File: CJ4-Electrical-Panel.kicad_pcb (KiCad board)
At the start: 2 copper layers, 122.4 x 62.5 mm, 43 parts, among them J1 Conn_01x03, J2 Conn_01x03, J3 Conn_01x03, J4 Conn_01x03, J5 Conn_01x03, J6 Conn_01x03, J7 USB_B_Mini, J8 AVR-ISP-6, U1 ATmega32U4-A, Y1 16MHz

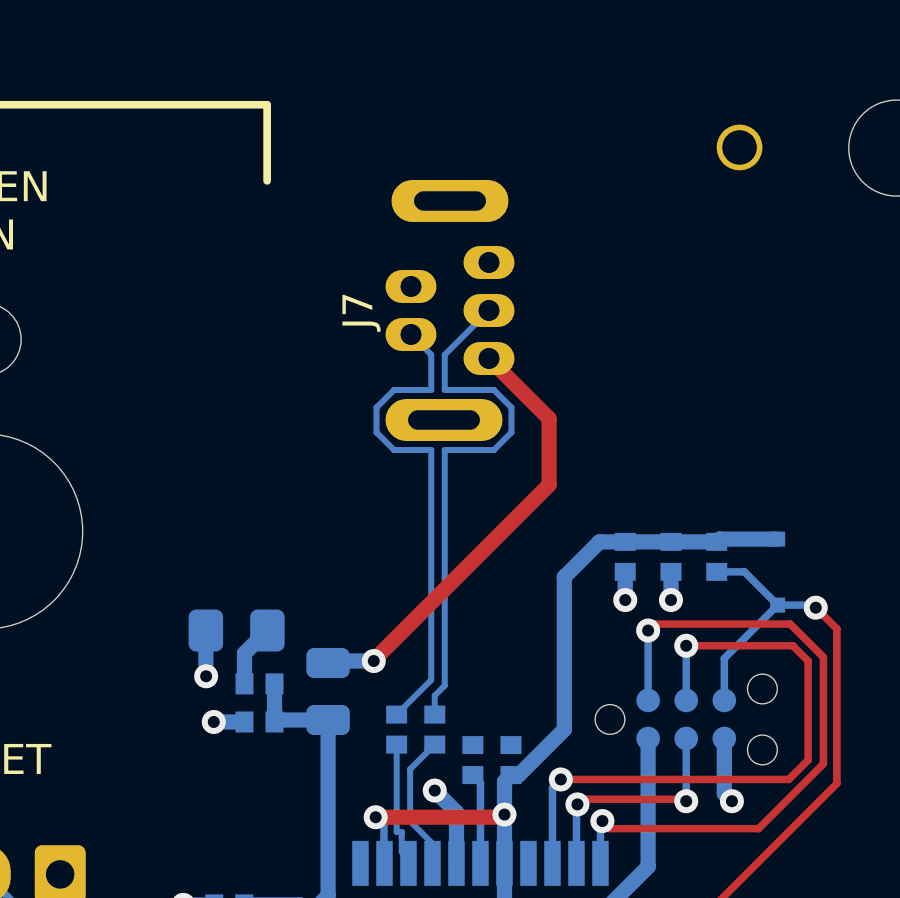
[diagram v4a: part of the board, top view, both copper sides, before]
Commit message: Move USB footprint to back of board
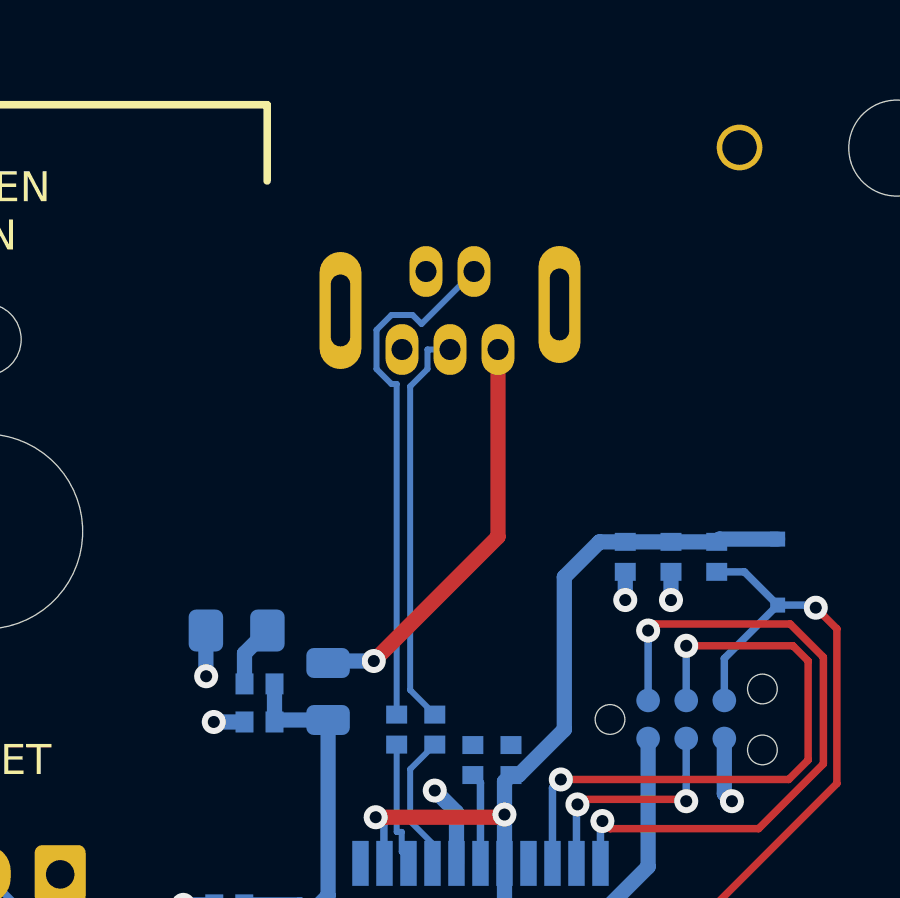
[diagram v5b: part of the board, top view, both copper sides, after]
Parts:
- J7: moved to B.Cu
- turned J7 to 0 degrees
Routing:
- net /DR+: track 18.0 -> 13.5 mm
- net /VBUS: track 14.9 -> 13.7 mm
- net /DR-: track 16.4 -> 17.5 mm
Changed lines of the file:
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@@
     )
-  )
-  (footprint "CJ4-Electrical-Panel:USB_B_Mini_Amphenol_UE25BE5510H" (layer "F.Cu")
-    (at 152.908 61.214 -90)
-    (property "Sheetfile" "CJ4-Electrical-Panel.kicad_sch")
-    (property "Sheetname" "")
-    (attr through_hole)
-    (fp_text reference "J7" (at 0 3.05 90) (layer "F.SilkS")
-      (effects (font (size 1 1) (thickness 0.15)))
-    )
-    (fp_text value "USB_B_Mini" (at 0 -3.25 90) (layer "F.Fab")
-      (effects (font (size 1 1) (thickness 0.15)))
-    )
-    (fp_line (start 3.85 -1.95) (end -3.85 -1.95) (layer "F.CrtYd") (width 0.12))
-    (fp_line (start -3.85 -1.95) (end -3.85 1.95) (layer "F.CrtYd") (width 0.12))
-    (fp_line (start -3.85 1.95) (end 3.85 1.95) (layer "F.CrtYd") (width 0.12))
-    (fp_line (start 3.85 1.95) (end 3.85 -1.95) (layer "F.CrtYd") (width 0.12))
-    (pad "1" thru_hole oval (at 1.6 -1.3 270) (size 1.1 1.7) (drill 0.7) (layers *.Cu *.Mask)
-      (net 32 "/VBUS") (pinfunction "VBUS") (pintype "power_out"))
-    (pad "2" thru_hole oval (at 0.8 1.3 270) (size 1.1 1.7) (drill 0.7) (layers *.Cu *.Mask)
-      (net 30 "/DR-") (pinfunction "D-") (pintype "bidirectional"))
-    (pad "3" thru_hole oval (at 0 -1.3 270) (size 1.1 1.7) (drill 0.7) (layers *.Cu *.Mask)
-      (net 31 "/DR+") (pinfunction "D+") (pintype "bidirectional"))
-    (pad "4" thru_hole oval (at -0.8 1.3 270) (size 1.1 1.7) (drill 0.7) (layers *.Cu *.Mask)
-      (net 29 "unconnected-(J7-Pad4)") (pinfunction "ID") (pintype "passive+no_connect"))
-    (pad "5" thru_hole oval (at -1.6 -1.3 270) (size 1.1 1.7) (drill 0.7) (layers *.Cu *.Mask)
-      (net 2 "GND") (pinfunction "GND") (pintype "power_out"))
-    (pad "6" thru_hole oval (at 3.65 0.2 270) (size 1.4 3.9) (drill oval 0.65 2.4) (layers *.Cu *.Mask)
-      (net 2 "GND") (pinfunction "Shield") (pintype "passive"))
-    (pad "6" thru_hole oval (at -3.65 0 270) (size 1.4 3.9) (drill oval 0.65 2.4) (layers *.Cu *.Mask)
-      (net 2 "GND") (pinfunction "Shield") (pintype "passive"))
   )
   (footprint "CJ4-Electrical-Panel:JLCPCB_Tooling_Hole" (layer "F.Cu")
@@
       (effects (font (size 0.5 0.5) (thickness 0.08)) (justify mirror))
     )
+    (fp_line (start -1.86 -0.96) (end 1 -0.96) (layer "B.SilkS") (width 0.12))
     (fp_line (start -1.86 0.96) (end -1.86 -0.96) (layer "B.SilkS") (width 0.12))
-    (fp_line (start -1.86 -0.96) (end 1 -0.96) (layer "B.SilkS") (width 0.12))
     (fp_line (start 1 0.96) (end -1.86 0.96) (layer "B.SilkS") (width 0.12))
     (fp_line (start -1.85 -0.95) (end -1.85 0.95) (layer "B.CrtYd") (width 0.05))
@@
     )
   )
+  (footprint "CJ4-Electrical-Panel:USB_B_Mini_Amphenol_UE25BE5510H" (layer "B.Cu")
+    (at 152.908 61.214)
+    (property "Sheetfile" "CJ4-Electrical-Panel.kicad_sch")
+    (property "Sheetname" "")
+    (attr through_hole)
+    (fp_text reference "J7" (at 0 -3.05) (layer "B.SilkS")
+      (effects (font (size 1 1) (thickness 0.15)) (justify mirror))
+    )
+    (fp_text value "USB_B_Mini" (at 0 3.25) (layer "B.Fab")
+      (effects (font (size 1 1) (thickness 0.15)) (justify mirror))
+    )
+    (fp_line (start 3.85 1.95) (end -3.85 1.95) (layer "B.CrtYd") (width 0.12))
+    (fp_line (start -3.85 1.95) (end -3.85 -1.95) (layer "B.CrtYd") (width 0.12))
+    (fp_line (start -3.85 -1.95) (end 3.85 -1.95) (layer "B.CrtYd") (width 0.12))
+    (fp_line (start 3.85 -1.95) (end 3.85 1.95) (layer "B.CrtYd") (width 0.12))
+    (pad "1" thru_hole oval (at 1.6 1.3) (size 1.1 1.7) (drill 0.7) (layers *.Cu *.Mask)
+      (net 32 "/VBUS") (pinfunction "VBUS") (pintype "power_out"))
+    (pad "2" thru_hole oval (at 0.8 -1.3) (size 1.1 1.7) (drill 0.7) (layers *.Cu *.Mask)
+      (net 30 "/DR-") (pinfunction "D-") (pintype "bidirectional"))
+    (pad "3" thru_hole oval (at 0 1.3) (size 1.1 1.7) (drill 0.7) (layers *.Cu *.Mask)
+      (net 31 "/DR+") (pinfunction "D+") (pintype "bidirectional"))
+    (pad "4" thru_hole oval (at -0.8 -1.3) (size 1.1 1.7) (drill 0.7) (layers *.Cu *.Mask)
+      (net 29 "unconnected-(J7-Pad4)") (pinfunction "ID") (pintype "passive+no_connect"))
+    (pad "5" thru_hole oval (at -1.6 1.3) (size 1.1 1.7) (drill 0.7) (layers *.Cu *.Mask)
+      (net 2 "GND") (pinfunction "GND") (pintype "power_out"))
+    (pad "6" thru_hole oval (at 3.65 -0.2) (size 1.4 3.9) (drill oval 0.65 2.4) (layers *.Cu *.Mask)
+      (net 2 "GND") (pinfunction "Shield") (pintype "passive"))
+    (pad "6" thru_hole oval (at -3.65 0) (size 1.4 3.9) (drill oval 0.65 2.4) (layers *.Cu *.Mask)
+      (net 2 "GND") (pinfunction "Shield") (pintype "passive"))
+  )
   (footprint "Connector_JST:JST_XH_B3B-XH-A_1x03_P2.50mm_Vertical" (layer "B.Cu")
     (at 139.914 80.01 180)
@@
   (gr_line (start 77.724 54.356) (end 77.724 56.896) (layer "F.SilkS") (width 0.254))
   (gr_line (start 50.8 53.34) (end 50.8 110.744) (layer "Edge.Cuts") (width 0.1))
+  (gr_line (start 53.34 113.284) (end 170.688 113.284) (layer "Edge.Cuts") (width 0.1))
   (gr_arc (start 50.8 53.34) (mid 51.543949 51.543949) (end 53.34 50.8) (layer "Edge.Cuts") (width 0.1))
   (gr_line (start 170.688 50.8) (end 53.34 50.8) (layer "Edge.Cuts") (width 0.1))
   (gr_line (start 173.228 110.744) (end 173.228 53.34) (layer "Edge.Cuts") (width 0.1))
-  (gr_line (start 53.34 113.284) (end 170.688 113.284) (layer "Edge.Cuts") (width 0.1))
   (gr_arc (start 170.688 50.8) (mid 172.484051 51.543949) (end 173.228 53.34) (layer "Edge.Cuts") (width 0.1))
   (gr_arc (start 173.228 110.744) (mid 172.484051 112.540051) (end 170.688 113.284) (layer "Edge.Cuts") (width 0.1))
@@
   (segment (start 113.077194 103.378) (end 109.521194 106.934) (width 0.25) (layer "B.Cu") (net 28))
   (segment (start 153.924 99.314) (end 149.86 103.378) (width 0.25) (layer "B.Cu") (net 28))
-  (segment (start 151.043986 63.86448) (end 152.282999 63.86448) (width 0.2) (layer "B.Cu") (net 30))
-  (segment (start 152.282999 62.688999) (end 151.608 62.014) (width 0.2) (layer "B.Cu") (net 30))
-  (segment (start 151.13 74.684) (end 152.282999 73.531001) (width 0.2) (layer "B.Cu") (net 30))
-  (segment (start 150.45848 64.449986) (end 151.043986 63.86448) (width 0.2) (layer "B.Cu") (net 30))
-  (segment (start 152.282999 63.86448) (end 152.282999 62.688999) (width 0.2) (layer "B.Cu") (net 30))
-  (segment (start 151.043986 65.86352) (end 150.45848 65.278014) (width 0.2) (layer "B.Cu") (net 30))
-  (segment (start 152.282999 65.86352) (end 151.043986 65.86352) (width 0.2) (layer "B.Cu") (net 30))
-  (segment (start 150.45848 65.278014) (end 150.45848 64.449986) (width 0.2) (layer "B.Cu") (net 30))
-  (segment (start 152.282999 73.531001) (end 152.282999 65.86352) (width 0.2) (layer "B.Cu") (net 30))
-  (segment (start 152.733001 73.717396) (end 152.733001 65.86352) (width 0.2) (layer "B.Cu") (net 31))
-  (segment (start 154.372014 65.86352) (end 154.95752 65.278014) (width 0.2) (layer "B.Cu") (net 31))
-  (segment (start 154.95752 64.449986) (end 154.372014 63.86448) (width 0.2) (layer "B.Cu") (net 31))
-  (segment (start 152.733001 63.86448) (end 152.733001 62.688999) (width 0.2) (layer "B.Cu") (net 31))
-  (segment (start 152.4 74.684) (end 152.4 74.050397) (width 0.2) (layer "B.Cu") (net 31))
-  (segment (start 154.372014 63.86448) (end 152.733001 63.86448) (width 0.2) (layer "B.Cu") (net 31))
-  (segment (start 152.733001 65.86352) (end 154.372014 65.86352) (width 0.2) (layer "B.Cu") (net 31))
-  (segment (start 154.95752 65.278014) (end 154.95752 64.449986) (width 0.2) (layer "B.Cu") (net 31))
-  (segment (start 152.4 74.050397) (end 152.733001 73.717396) (width 0.2) (layer "B.Cu") (net 31))
-  (segment (start 152.733001 62.688999) (end 154.208 61.214) (width 0.2) (layer "B.Cu") (net 31))
-  (segment (start 150.368 72.898) (end 150.368 72.871323) (width 0.508) (layer "F.Cu") (net 32))
-  (segment (start 156.21 64.816) (end 154.208 62.814) (width 0.508) (layer "F.Cu") (net 32))
-  (segment (start 150.368 72.871323) (end 156.21 67.029323) (width 0.508) (layer "F.Cu") (net 32))
-  (segment (start 156.21 67.029323) (end 156.21 64.816) (width 0.508) (layer "F.Cu") (net 32))
+  (segment (start 151.13 63.66352) (end 151.13 74.684) (width 0.2) (layer "B.Cu") (net 30))
+  (segment (start 150.45848 61.862118) (end 150.45848 63.165882) (width 0.2) (layer "B.Cu") (net 30))
+  (segment (start 150.956118 63.66352) (end 151.13 63.66352) (width 0.2) (layer "B.Cu") (net 30))
+  (segment (start 151.958701 61.663299) (end 151.659882 61.36448) (width 0.2) (layer "B.Cu") (net 30))
+  (segment (start 150.45848 63.165882) (end 150.956118 63.66352) (width 0.2) (layer "B.Cu") (net 30))
+  (segment (start 150.956118 61.36448) (end 150.45848 61.862118) (width 0.2) (layer "B.Cu") (net 30))
+  (segment (start 153.708 59.914) (end 151.958701 61.663299) (width 0.2) (layer "B.Cu") (net 30))
+  (segment (start 151.659882 61.36448) (end 150.956118 61.36448) (width 0.2) (layer "B.Cu") (net 30))
+  (segment (start 152.15752 63.165882) (end 151.580001 63.743401) (width 0.2) (layer "B.Cu") (net 31))
+  (segment (start 151.580001 63.743401) (end 151.580001 73.864001) (width 0.2) (layer "B.Cu") (net 31))
+  (segment (start 152.15752 62.514) (end 152.15752 63.165882) (width 0.2) (layer "B.Cu") (net 31))
+  (segment (start 151.580001 73.864001) (end 152.4 74.684) (width 0.2) (layer "B.Cu") (net 31))
+  (segment (start 152.908 62.514) (end 152.15752 62.514) (width 0.2) (layer "B.Cu") (net 31))
+  (segment (start 154.508 68.758) (end 150.368 72.898) (width 0.508) (layer "F.Cu") (net 32))
+  (segment (start 154.508 62.514) (end 154.508 68.758) (width 0.508) (layer "F.Cu") (net 32))
   (via (at 150.368 72.898) (size 0.8) (drill 0.4) (layers "F.Cu" "B.Cu") (net 32))
   (segment (start 148.91 72.898) (end 148.844 72.964) (width 0.508) (layer "B.Cu") (net 32))
